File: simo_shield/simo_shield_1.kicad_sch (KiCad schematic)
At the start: 6 parts, among them J1 CONECTOR DEBUG_UART, J2 VBAT, U1 YAAJ_BluePill_Part_Like_SWD_B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, U2 elemon_board, U3 flash_externa, U4 mpu6050

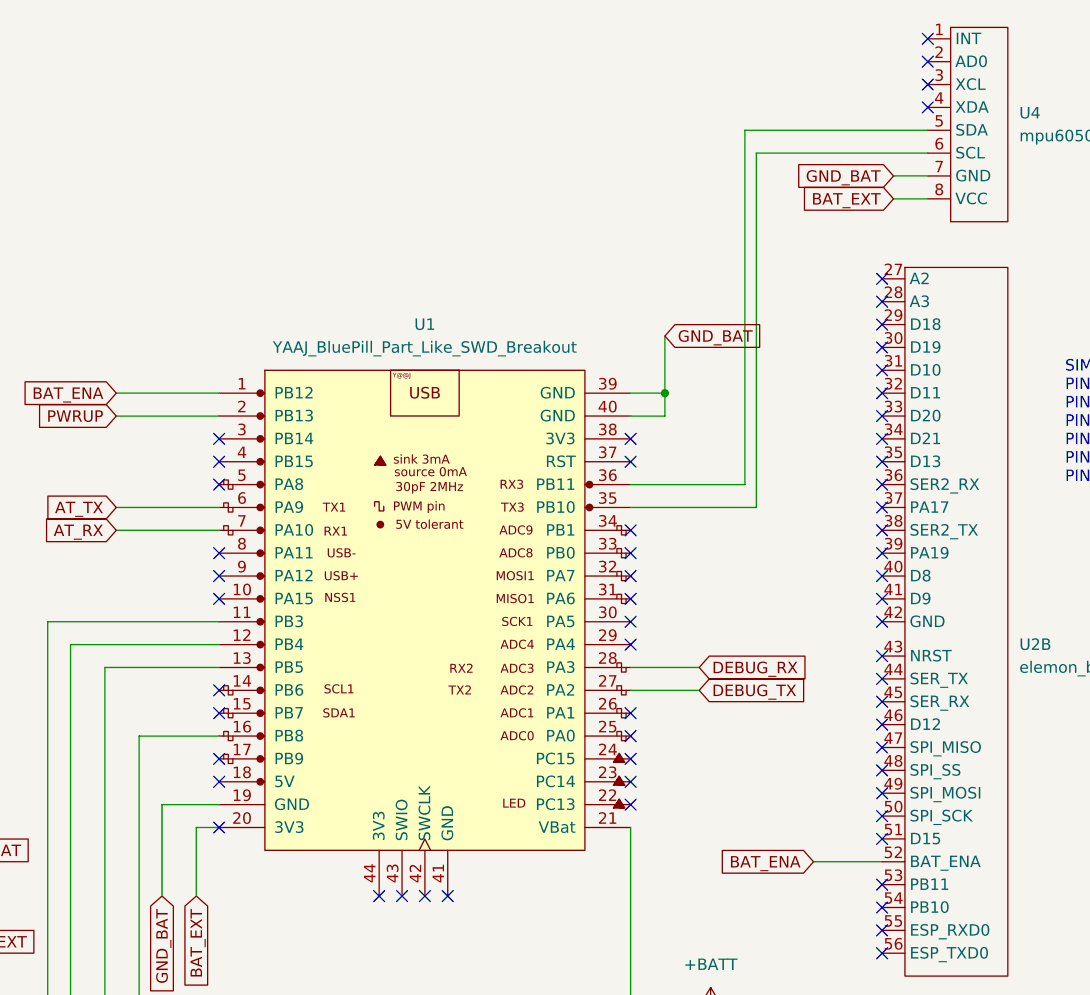
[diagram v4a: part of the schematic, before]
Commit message: en esquematico pin 35 y 36 se conectan con SDA y SCL de MPU6050. En PCB no aparece tal conexion
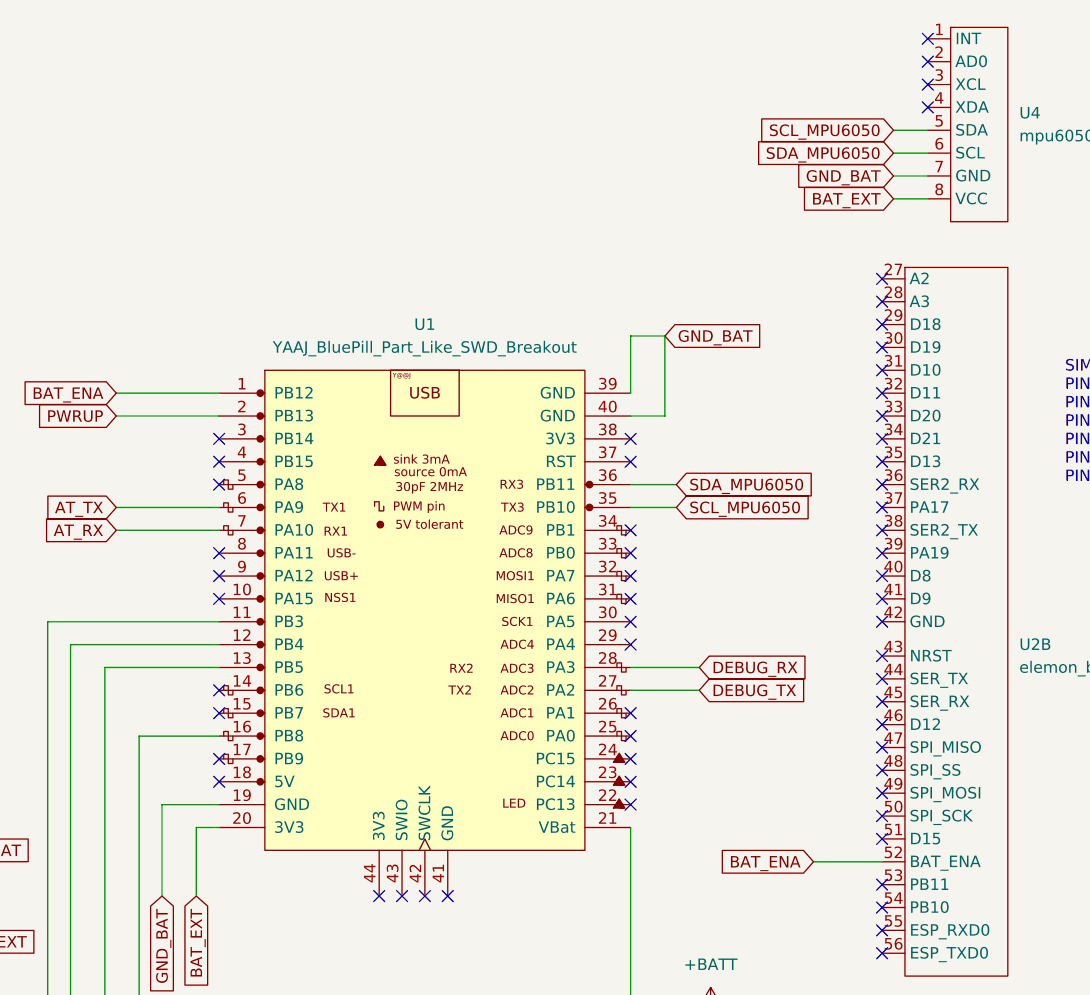
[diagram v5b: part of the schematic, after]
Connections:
- net SCL_MPU6050: now reaches U1.35 (PB10)
- net SCL_MPU6050: now also U4.5 (SDA); no longer U4.6 (SCL)
- net SDA_MPU6050: now reaches U1.36 (PB11)
- net SDA_MPU6050: now also U4.6 (SCL); no longer U4.5 (SDA)
- no-connect marks 83 -> 82
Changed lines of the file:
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@@
   (junction (at 170.18 134.62) (diameter 0) (color 0 0 0 0)
-  )
-  (junction (at 165.1 59.69) (diameter 0) (color 0 0 0 0)
   )
   (junction (at 161.29 132.08) (diameter 0) (color 0 0 0 0)
@@
   (no_connect (at 189.23 91.44))
   (no_connect (at 161.29 82.55))
-  (no_connect (at 115.57 107.95))
   (no_connect (at 161.29 64.77))
   (wire (pts (xy 62.23 53.34) (xy 76.2 53.34))
@@
     (stroke (width 0) (type default) (color 0 0 0 0))
   )
-  (wire (pts (xy 165.1 59.69) (xy 165.1 62.23))
+  (wire (pts (xy 161.29 62.23) (xy 165.1 62.23))
+    (stroke (width 0) (type default) (color 0 0 0 0))
+  )
+  (wire (pts (xy 161.29 53.34) (xy 165.1 53.34))
     (stroke (width 0) (type default) (color 0 0 0 0))
   )
@@
     (stroke (width 0) (type default) (color 0 0 0 0))
   )
+  (wire (pts (xy 113.03 107.95) (xy 113.03 115.57))
+    (stroke (width 0) (type default) (color 0 0 0 0))
+  )
   (wire (pts (xy 80.01 115.57) (xy 80.01 120.65))
     (stroke (width 0) (type default) (color 0 0 0 0))
@@
     (stroke (width 0) (type default) (color 0 0 0 0))
   )
-  (wire (pts (xy 161.29 69.85) (xy 173.99 69.85))
+  (wire (pts (xy 115.57 107.95) (xy 113.03 107.95))
     (stroke (width 0) (type default) (color 0 0 0 0))
   )
@@
     (stroke (width 0) (type default) (color 0 0 0 0))
   )
-  (wire (pts (xy 115.57 105.41) (xy 109.22 105.41))
+  (wire (pts (xy 161.29 72.39) (xy 166.37 72.39))
     (stroke (width 0) (type default) (color 0 0 0 0))
   )
@@
     (stroke (width 0) (type default) (color 0 0 0 0))
   )
-  (wire (pts (xy 175.26 33.02) (xy 194.31 33.02))
-    (stroke (width 0) (type default) (color 0 0 0 0))
-  )
-  (wire (pts (xy 113.03 107.95) (xy 113.03 115.57))
-    (stroke (width 0) (type default) (color 0 0 0 0))
-  )
   (wire (pts (xy 96.52 85.09) (xy 115.57 85.09))
     (stroke (width 0) (type default) (color 0 0 0 0))
   )
-  (wire (pts (xy 115.57 107.95) (xy 113.03 107.95))
-    (stroke (width 0) (type default) (color 0 0 0 0))
-  )
-  (wire (pts (xy 173.99 30.48) (xy 194.31 30.48))
-    (stroke (width 0) (type default) (color 0 0 0 0))
-  )
   (wire (pts (xy 109.22 105.41) (xy 109.22 115.57))
     (stroke (width 0) (type default) (color 0 0 0 0))
@@
     (stroke (width 0) (type default) (color 0 0 0 0))
   )
-  (wire (pts (xy 161.29 72.39) (xy 175.26 72.39))
+  (wire (pts (xy 165.1 53.34) (xy 165.1 62.23))
     (stroke (width 0) (type default) (color 0 0 0 0))
   )
@@
     (stroke (width 0) (type default) (color 0 0 0 0))
   )
+  (wire (pts (xy 190.5 33.02) (xy 194.31 33.02))
+    (stroke (width 0) (type default) (color 0 0 0 0))
+  )
   (wire (pts (xy 73.66 137.16) (xy 99.06 137.16))
     (stroke (width 0) (type default) (color 0 0 0 0))
   )
-  (wire (pts (xy 173.99 69.85) (xy 173.99 30.48))
+  (wire (pts (xy 190.5 30.48) (xy 194.31 30.48))
     (stroke (width 0) (type default) (color 0 0 0 0))
   )
@@
     (stroke (width 0) (type default) (color 0 0 0 0))
   )
-  (wire (pts (xy 161.29 62.23) (xy 165.1 62.23))
-    (stroke (width 0) (type default) (color 0 0 0 0))
-  )
   (wire (pts (xy 165.1 134.62) (xy 165.1 144.78))
     (stroke (width 0) (type default) (color 0 0 0 0))
@@
     (stroke (width 0) (type default) (color 0 0 0 0))
   )
-  (wire (pts (xy 165.1 53.34) (xy 165.1 59.69))
-    (stroke (width 0) (type default) (color 0 0 0 0))
-  )
   (wire (pts (xy 170.18 128.27) (xy 170.18 132.08))
     (stroke (width 0) (type default) (color 0 0 0 0))
@@
     (stroke (width 0) (type default) (color 0 0 0 0))
   )
-  (wire (pts (xy 175.26 33.02) (xy 175.26 72.39))
+  (wire (pts (xy 161.29 69.85) (xy 166.37 69.85))
+    (stroke (width 0) (type default) (color 0 0 0 0))
+  )
+  (wire (pts (xy 161.29 59.69) (xy 161.29 53.34))
+    (stroke (width 0) (type default) (color 0 0 0 0))
+  )
+  (wire (pts (xy 109.22 105.41) (xy 115.57 105.41))
     (stroke (width 0) (type default) (color 0 0 0 0))
   )
@@
   )
   (wire (pts (xy 161.29 132.08) (xy 161.29 144.78))
-    (stroke (width 0) (type default) (color 0 0 0 0))
-  )
-  (wire (pts (xy 161.29 59.69) (xy 165.1 59.69))
     (stroke (width 0) (type default) (color 0 0 0 0))
   )
@@
     (effects (font (size 1.27 1.27)) (justify left bottom))
   )
+  (global_label "SDA_MPU6050" (shape input) (at 166.37 69.85 0) (fields_autoplaced)
+    (effects (font (size 1.27 1.27)) (justify left))
+    (property "Referencias entre hojas" "${INTERSHEET_REFS}" (id 0) (at 182.2088 69.9294 0)
+      (effects (font (size 1.27 1.27)) (justify left) hide)
+    )
+  )
   (global_label "AT_TX" (shape input) (at 104.14 72.39 180) (fields_autoplaced)
     (effects (font (size 1.27 1.27)) (justify right))
@@
     )
   )
+  (global_label "SDA_MPU6050" (shape input) (at 190.5 33.02 180) (fields_autoplaced)
+    (effects (font (size 1.27 1.27)) (justify right))
+    (property "Referencias entre hojas" "${INTERSHEET_REFS}" (id 0) (at 174.6612 32.9406 0)
+      (effects (font (size 1.27 1.27)) (justify right) hide)
+    )
+  )
+  (global_label "SCL_MPU6050" (shape input) (at 166.37 72.39 0) (fields_autoplaced)
+    (effects (font (size 1.27 1.27)) (justify left))
+    (property "Referencias entre hojas" "${INTERSHEET_REFS}" (id 0) (at 182.1483 72.4694 0)
+      (effects (font (size 1.27 1.27)) (justify left) hide)
+    )
+  )
   (global_label "BAT_ENA" (shape input) (at 181.61 111.76 180) (fields_autoplaced)
     (effects (font (size 1.27 1.27)) (justify right))
@@
     )
   )
+  (global_label "SCL_MPU6050" (shape input) (at 190.5 30.48 180) (fields_autoplaced)
+    (effects (font (size 1.27 1.27)) (justify right))
+    (property "Referencias entre hojas" "${INTERSHEET_REFS}" (id 0) (at 174.7217 30.4006 0)
+      (effects (font (size 1.27 1.27)) (justify right) hide)
+    )
+  )

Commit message: casi terminado, revisar PCB, error de conexion pero no entiendo por que.
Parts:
- U1: footprint simo:YAAJ_BluePill_SWD_1 -> bluepill:YAAJ_BluePill_SWD_1
- renumbered J2 to CONECTOR_BATERIA1
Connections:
- net +BATT: no longer U1.20 (3V3)
- net AT_RX: no longer names the net of U1.7 (PA10), U2.2 (SER3_TX)
- net AT_TX: no longer names the net of U1.6 (PA9), U2.4 (SER3_RX)
- net BAT_ENA renamed BAT_ENA_PIN
- net DEBUG_RX: no longer names the net of J1.2 (Pin_2)
- net DEBUG_RX: now also U1.27 (PA2); no longer U1.28 (PA3)
- net DEBUG_TX: no longer names the net of J1.1 (Pin_1)
- net DEBUG_TX: now also U1.28 (PA3); no longer U1.27 (PA2)
- net GND renamed BAT_GND
- net PWRUP: no longer names the net of U1.2 (PB13), U2.9 (PWRKEY)
- net SCL_MPU6050: no longer names the net of U1.35 (PB10)
- net SCL_MPU6050: now also U4.6 (SCL); no longer U4.5 (SDA)
- net SDA_MPU6050: no longer names the net of U1.36 (PB11)
- net SDA_MPU6050: now also U4.5 (SDA); no longer U4.6 (SCL)
- no-connect marks 82 -> 83
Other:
- note added: "CONECTOR BATERIA, INCLUYE REGULADORES"
- note added: "CONECTOR DE SALIDA DEL UART_DEBUG DEL PROGRAMA"
- moved on the sheet: CONECTOR_BATERIA1, J1, U1, U2A, U2B, U3, U4

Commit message: update en pcb shield
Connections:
- net at U1.10 (PA15): now also U2.14 (RI)
- no-connect marks 83 -> 81
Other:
- note added: "SIM7000G: PIN_SIM_BAT ------> PB12 PIN_SIM_PWRUP ------> PB13 PIN_AT_TX ------> PA10 PIN_AT_RX ------> PA9 PIN_DEGUG_TX ------> PA2 PIN_DEBUG_RX ------> PA3 PIN_RI -------PA15"
- note removed: "SIM7000G: PIN_SIM_BAT ------> PB12 PIN_SIM_PWRUP ------> PB13 PIN_AT_TX ------> PA10 PIN_AT_RX ------> PA9 PIN_DEGUG_TX ------> PA2 PIN_DEBUG_RX ------> PA3"
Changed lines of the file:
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@@
   (no_connect (at 132.08 69.85))
   (no_connect (at 132.08 77.47))
-  (no_connect (at 132.08 82.55))
   (no_connect (at 132.08 80.01))
   (no_connect (at 132.08 67.31))
-  (no_connect (at 132.08 64.77))
   (no_connect (at 132.08 95.25))
   (no_connect (at 132.08 92.71))
@@
   (no_connect (at 177.8 97.79))
   (no_connect (at 177.8 95.25))
+  (no_connect (at 132.08 64.77))
   (no_connect (at 177.8 87.63))
   (no_connect (at 177.8 77.47))
@@
   (no_connect (at 72.39 73.66))
   (no_connect (at 72.39 86.36))
-  (no_connect (at 72.39 81.28))
   (no_connect (at 72.39 76.2))
   (no_connect (at 72.39 91.44))
@@
     (stroke (width 0) (type default) (color 0 0 0 0))
   )
+  (wire (pts (xy 99.06 82.55) (xy 99.06 81.28))
+    (stroke (width 0) (type default) (color 0 0 0 0))
+  )
   (wire (pts (xy 55.88 134.62) (xy 67.31 134.62))
     (stroke (width 0) (type default) (color 0 0 0 0))
@@
     (stroke (width 0) (type default) (color 0 0 0 0))
   )
+  (wire (pts (xy 132.08 82.55) (xy 99.06 82.55))
+    (stroke (width 0) (type default) (color 0 0 0 0))
+  )
   (wire (pts (xy 34.29 105.41) (xy 39.37 105.41))
     (stroke (width 0) (type default) (color 0 0 0 0))
@@
   )
   (wire (pts (xy 128.27 105.41) (xy 132.08 105.41))
+    (stroke (width 0) (type default) (color 0 0 0 0))
+  )
+  (wire (pts (xy 72.39 81.28) (xy 99.06 81.28))
     (stroke (width 0) (type default) (color 0 0 0 0))
   )
@@
     (effects (font (size 1.27 1.27)) (justify left bottom))
   )
-  (text "SIM7000G:\nPIN_SIM_BAT      ------> PB12\nPIN_SIM_PWRUP   ------> PB13\nPIN_AT_TX	   ------> PA10\nPIN_AT_RX	   ------> PA9\nPIN_DEGUG_TX    ------> PA2\nPIN_DEBUG_RX    ------> PA3"
+  (text "SIM7000G:\nPIN_SIM_BAT      ------> PB12\nPIN_SIM_PWRUP   ------> PB13\nPIN_AT_TX	   ------> PA10\nPIN_AT_RX	   ------> PA9\nPIN_DEGUG_TX    ------> PA2\nPIN_DEBUG_RX    ------> PA3\nPIN_RI			-------PA15"
     (at 38.1 29.21 0)
     (effects (font (size 1.27 1.27)) (justify left bottom))

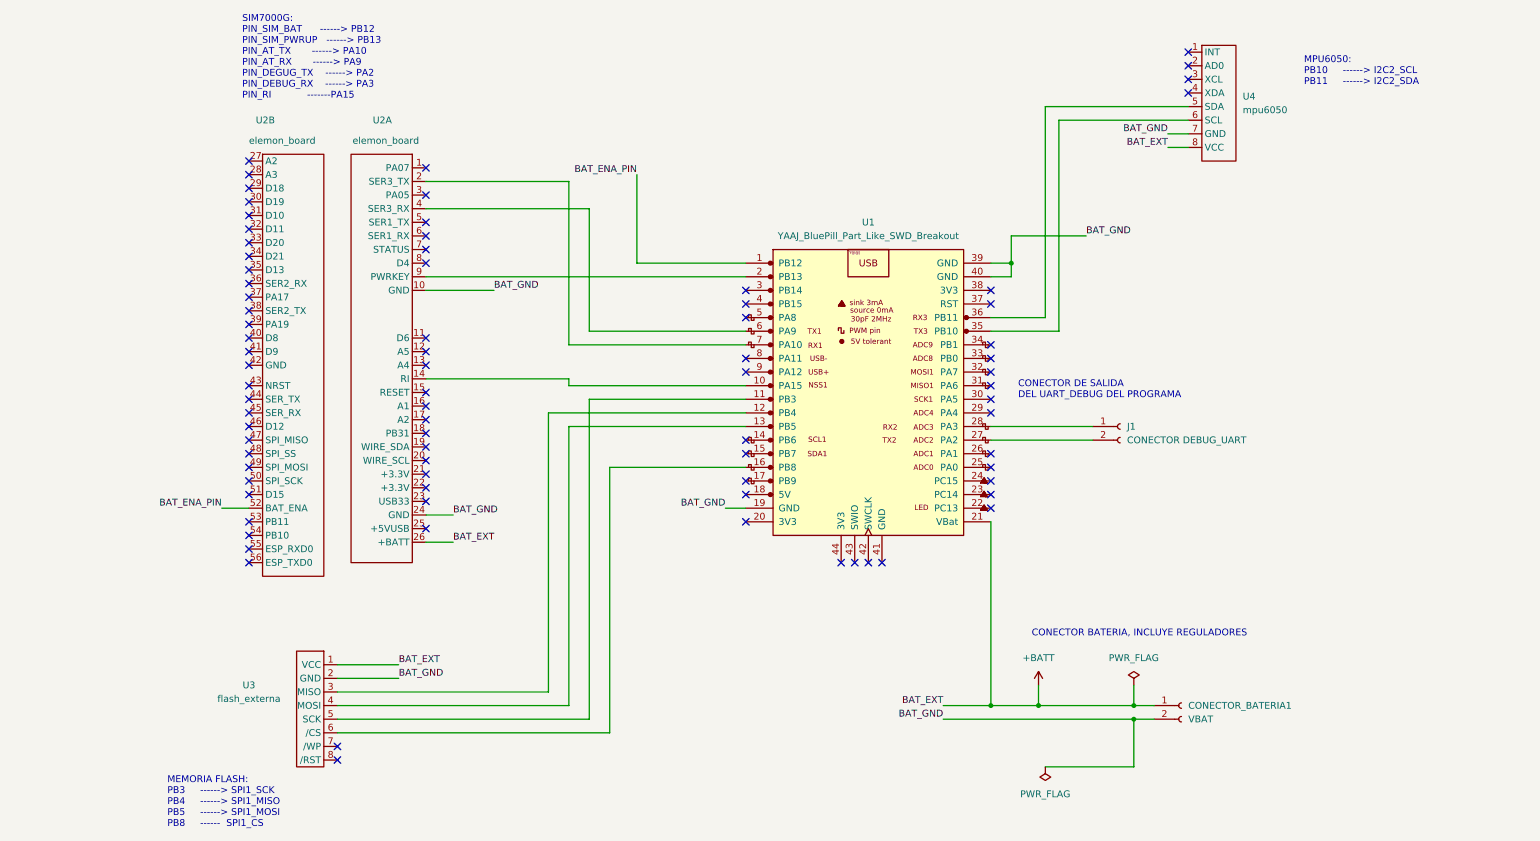
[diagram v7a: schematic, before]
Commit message: se agrego un circuito para mediciones de tension de bateria mediante la bluepill
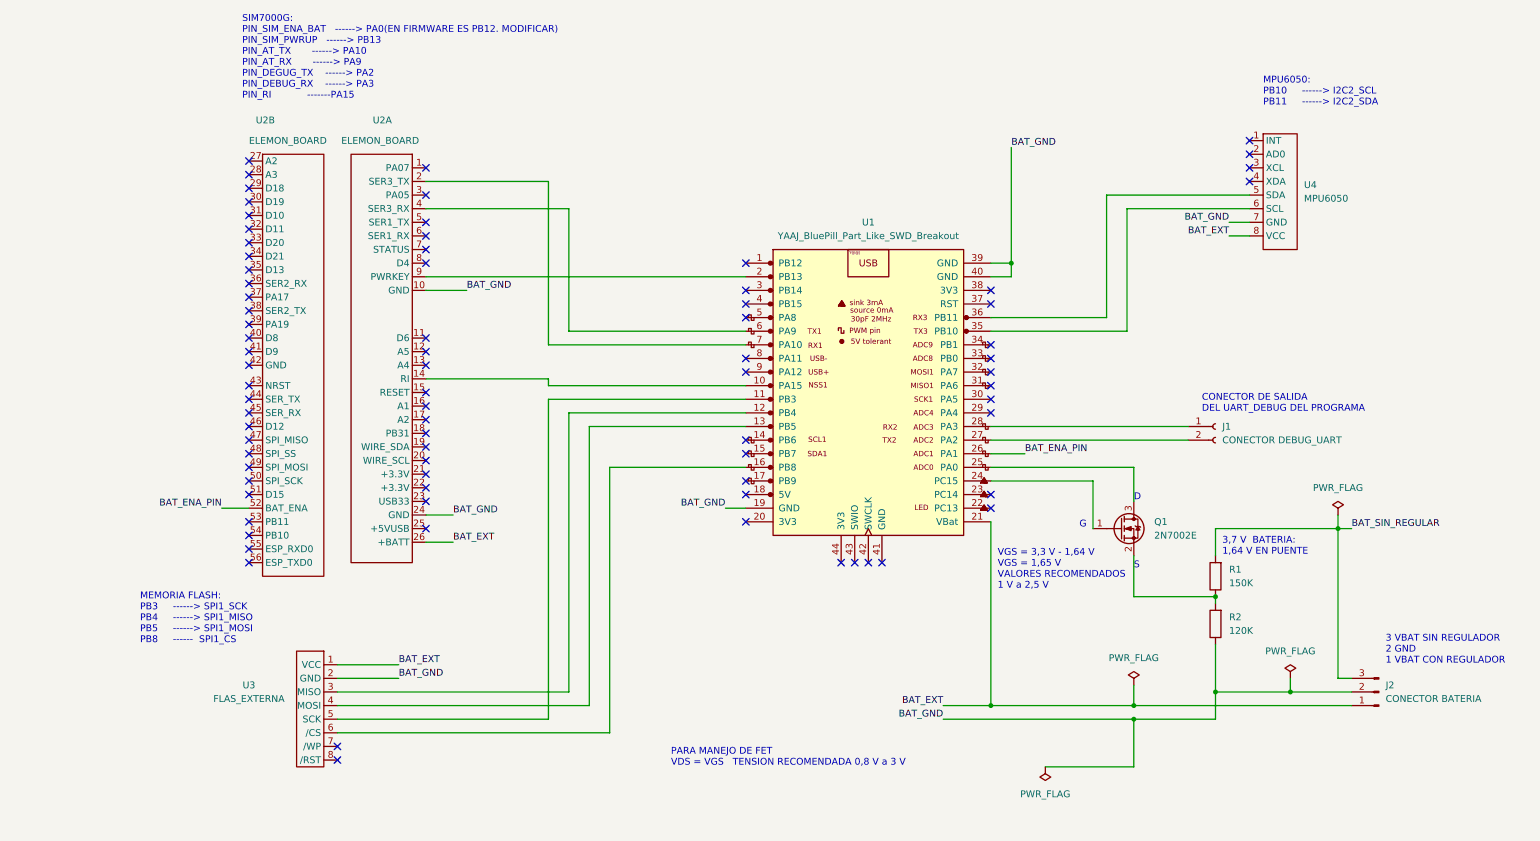
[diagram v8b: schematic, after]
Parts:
- removed CONECTOR_BATERIA1: VBAT, Connector_JST:JST_EH_B2B-EH-A_1x02_P2.50mm_Vertical, symbol Connector:Conn_01x02_Female
- added J2: CONECTOR BATERIA, Connector_JST:JST_EH_B3B-EH-A_1x03_P2.50mm_Vertical, symbol Connector:Conn_01x03_Male
- added Q1: 2N7002E, Package_TO_SOT_SMD:SOT-23, symbol Transistor_FET:2N7002E
- added R1: 150K, Resistor_SMD:R_0805_2012Metric, symbol Device:R
- added R2: 120K, Resistor_SMD:R_0805_2012Metric, symbol Device:R
- U1: footprint bluepill:YAAJ_BluePill_SWD_1 -> bluepill:YAAJ_BluePill_SWD_1_modificado
- U2: value elemon_board -> ELEMON_BOARD; footprint elemon_board:elemon_board -> elemon_board:elemon_board_modificado; Descripcion (none) -> Modulo de comunicacion 4G basado en SIM7000G
- U3: value flash_externa -> FLAS_EXTERNA; Descripcion (none) -> Modulo tipo Arduino con memoria flash externa AT45DB0E41
- U4: value mpu6050 -> MPU6050; Descripcion (none) -> Modulo acelerometro tipo arduino. 3 eje , giroscopio y temp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; Digikey (none) -> 2234-BAL-01-ND; Factory number (none) -> BAL-01
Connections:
- net BAT_ENA_PIN: now also U1.26 (PA1); no longer U1.1 (PB12)
- net BAT_GND: now also J2.2 (Pin_2), R2.1
- net at U1.24 (PC15): now also Q1.1 (G)
- net at U1.25 (PA0): now also Q1.3 (D)
- net +BATT renamed BAT_EXT
- net BAT_EXT: now also J2.1 (Pin_1)
- new net: Q1.2 (S), R1.1, R2.2
- new net BAT_SIN_REGULAR: J2.3 (Pin_3), R1.2
- no-connect marks 81 -> 79
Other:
- note added: "3 VBAT SIN REGULADOR 2 GND 1 VBAT CON REGULADOR"
- note added: "3,7 V BATERIA: 1,64 V EN PUENTE"
- note added: "D"
- note added: "G"
- note added: "PARA MANEJO DE FET VDS = VGS TENSION RECOMENDADA 0,8 V a 3 V"
- note added: "S"
- note added: "SIM7000G: PIN_SIM_ENA_BAT ------> PA0(EN FIRMWARE ES PB12. MODIFICAR) PIN_SIM_PWRUP ------> PB13 PIN_AT_TX ------> PA10 PIN_AT_RX ------> PA9 PIN_DEGUG_TX ------> PA2 PIN_DEBUG_RX ------> PA3 PIN_RI -------PA15"
- note added: "VGS = 3,3 V - 1,64 V VGS = 1,65 V VALORES RECOMENDADOS 1 V a 2,5 V"
- note removed: "CONECTOR BATERIA, INCLUYE REGULADORES"
- note removed: "SIM7000G: PIN_SIM_BAT ------> PB12 PIN_SIM_PWRUP ------> PB13 PIN_AT_TX ------> PA10 PIN_AT_RX ------> PA9 PIN_DEGUG_TX ------> PA2 PIN_DEBUG_RX ------> PA3 PIN_RI -------PA15"
- company: (none) -> I.N.T.I
- title: (none) -> Simo Shield, PCB de conexion
- moved on the sheet: J1, U4
